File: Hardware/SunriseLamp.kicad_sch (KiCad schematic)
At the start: 0 parts

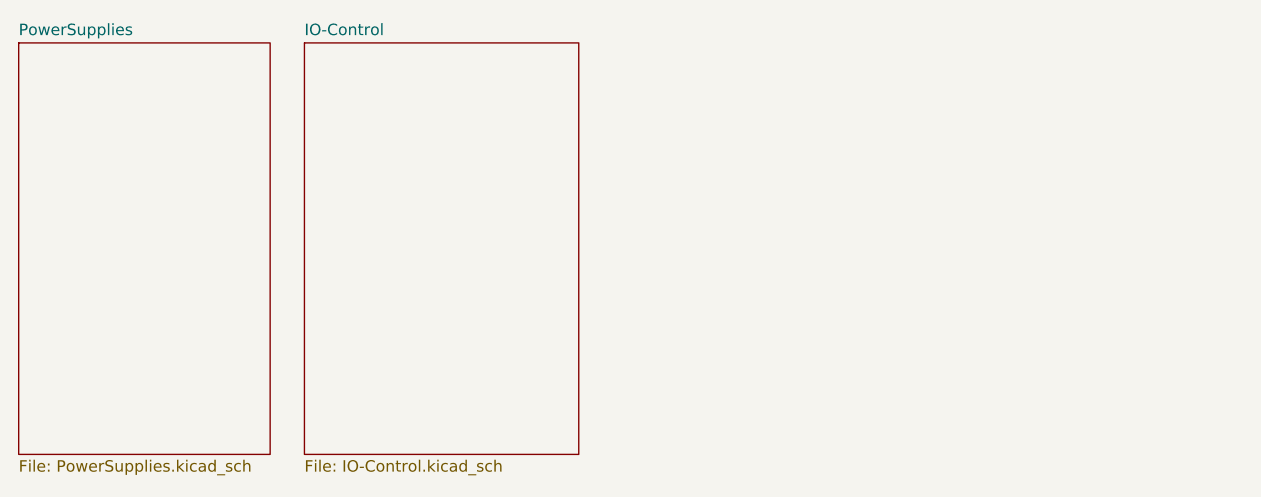
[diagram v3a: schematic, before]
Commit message: USB footprint added, mount holes added.
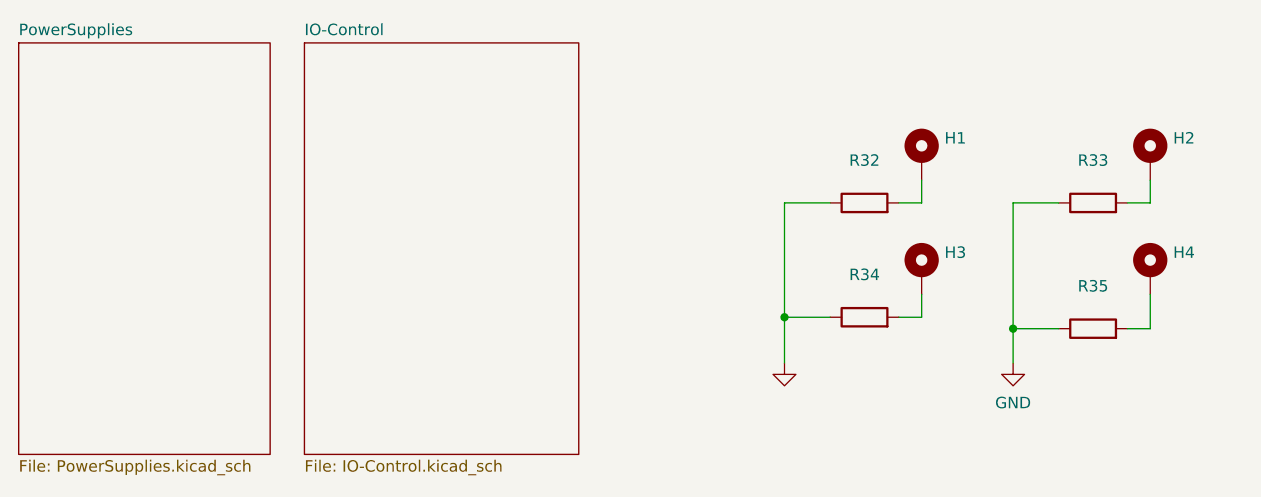
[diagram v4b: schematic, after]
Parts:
- added H1, H2, H3, H4: (no value), symbol Mechanical:MountingHole_Pad
- added R32, R33, R34, R35: (no value), symbol Device:R
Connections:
- new net: H3.1, R34.2
- new net: H1.1, R32.2
- new net: H4.1, R35.2
- new net: H2.1, R33.2
- new net GND: R32.1, R33.1, R34.1, R35.1

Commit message: Whoops, acidentally wiped all part assignments somehow. corrected.
Only pending footprint creation is for two switches.
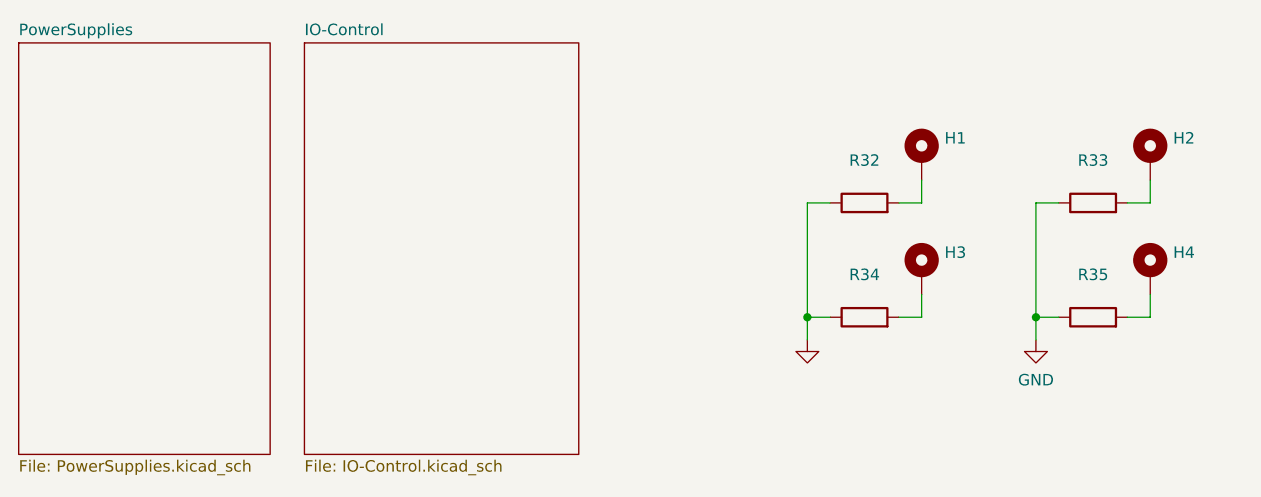
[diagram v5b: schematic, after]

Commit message: Layout changes
Changed XT60 outputs to Mini-Fit Jr., laid out 80mm fan edge cuts, started positioning conns
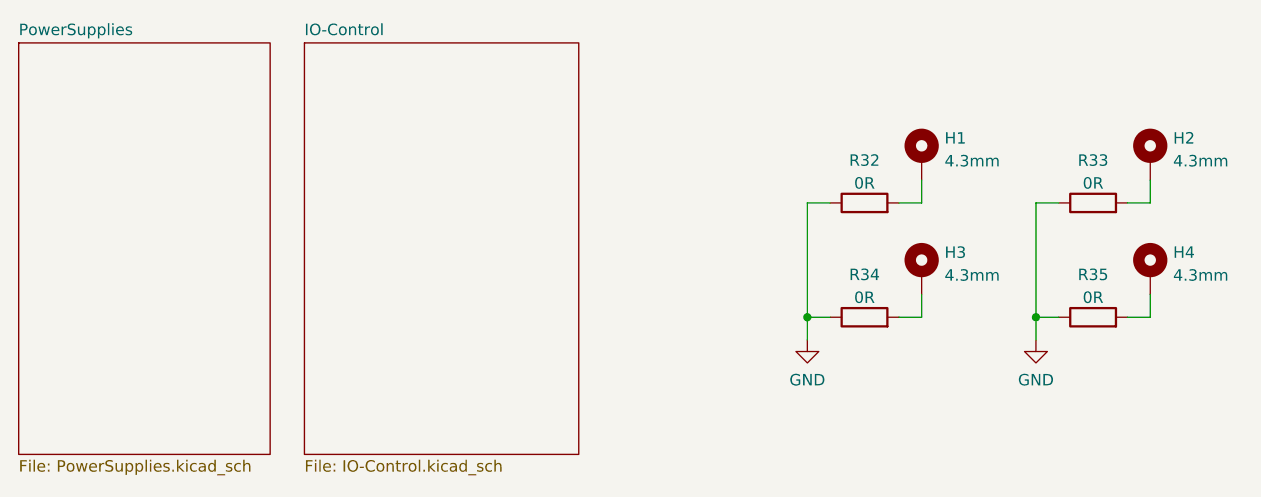
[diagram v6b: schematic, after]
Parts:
- H1, H2, H3, H4: value (none) -> 4.3mm; footprint (none) -> MountingHole:MountingHole_4.3mm_M4_DIN965_Pad_TopBottom
- R32, R33, R34, R35: value (none) -> 0R; footprint (none) -> Resistor_SMD:R_0805_2012Metric_Pad1.20x1.40mm_HandSolder
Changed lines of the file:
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@@
     (in_bom yes) (on_board yes) (fields_autoplaced)
     (property "Reference" "R35" (id 0) (at 146.05 52.4342 90))
-    (property "Value" "" (id 1) (at 146.05 54.9711 90))
-    (property "Footprint" "" (id 2) (at 146.05 58.928 90)
+    (property "Value" "0R" (id 1) (at 146.05 54.9711 90))
+    (property "Footprint" "Resistor_SMD:R_0805_2012Metric_Pad1.20x1.40mm_HandSolder" (id 2) (at 146.05 58.928 90)
       (effects (font (size 1.27 1.27)) hide)
     )
@@
     (in_bom yes) (on_board yes) (fields_autoplaced)
     (property "Reference" "R34" (id 0) (at 120.65 52.4342 90))
-    (property "Value" "" (id 1) (at 120.65 54.9711 90))
-    (property "Footprint" "" (id 2) (at 120.65 58.928 90)
+    (property "Value" "0R" (id 1) (at 120.65 54.9711 90))
+    (property "Footprint" "Resistor_SMD:R_0805_2012Metric_Pad1.20x1.40mm_HandSolder" (id 2) (at 120.65 58.928 90)
       (effects (font (size 1.27 1.27)) hide)
     )
@@
     (in_bom yes) (on_board yes) (fields_autoplaced)
     (property "Reference" "R33" (id 0) (at 146.05 39.7342 90))
-    (property "Value" "" (id 1) (at 146.05 42.2711 90))
-    (property "Footprint" "" (id 2) (at 146.05 46.228 90)
+    (property "Value" "0R" (id 1) (at 146.05 42.2711 90))
+    (property "Footprint" "Resistor_SMD:R_0805_2012Metric_Pad1.20x1.40mm_HandSolder" (id 2) (at 146.05 46.228 90)
       (effects (font (size 1.27 1.27)) hide)
     )
@@
       (effects (font (size 1.27 1.27)) (justify left))
     )
-    (property "Value" "" (id 1) (at 129.54 39.8022 0)
-      (effects (font (size 1.27 1.27)) (justify left))
-    )
-    (property "Footprint" "" (id 2) (at 127 39.37 0)
+    (property "Value" "4.3mm" (id 1) (at 129.54 39.8022 0)
+      (effects (font (size 1.27 1.27)) (justify left))
+    )
+    (property "Footprint" "MountingHole:MountingHole_4.3mm_M4_DIN965_Pad_TopBottom" (id 2) (at 127 39.37 0)
       (effects (font (size 1.27 1.27)) hide)
     )
@@
       (effects (font (size 1.27 1.27)) (justify left))
     )
-    (property "Value" "" (id 1) (at 154.94 39.8022 0)
-      (effects (font (size 1.27 1.27)) (justify left))
-    )
-    (property "Footprint" "" (id 2) (at 152.4 39.37 0)
+    (property "Value" "4.3mm" (id 1) (at 154.94 39.8022 0)
+      (effects (font (size 1.27 1.27)) (justify left))
+    )
+    (property "Footprint" "MountingHole:MountingHole_4.3mm_M4_DIN965_Pad_TopBottom" (id 2) (at 152.4 39.37 0)
       (effects (font (size 1.27 1.27)) hide)
     )
@@
       (effects (font (size 1.27 1.27)) hide)
     )
-    (property "Value" "" (id 1) (at 114.3 64.1334 0))
+    (property "Value" "GND" (id 1) (at 114.3 64.1334 0))
     (property "Footprint" "" (id 2) (at 114.3 59.69 0)
       (effects (font (size 1.27 1.27)) hide)
@@
       (effects (font (size 1.27 1.27)) (justify left))
     )
-    (property "Value" "" (id 1) (at 129.54 52.5022 0)
-      (effects (font (size 1.27 1.27)) (justify left))
-    )
-    (property "Footprint" "" (id 2) (at 127 52.07 0)
+    (property "Value" "4.3mm" (id 1) (at 129.54 52.5022 0)
+      (effects (font (size 1.27 1.27)) (justify left))
+    )
+    (property "Footprint" "MountingHole:MountingHole_4.3mm_M4_DIN965_Pad_TopBottom" (id 2) (at 127 52.07 0)
       (effects (font (size 1.27 1.27)) hide)
     )
@@
       (effects (font (size 1.27 1.27)) (justify left))
     )
-    (property "Value" "" (id 1) (at 154.94 52.5022 0)
-      (effects (font (size 1.27 1.27)) (justify left))
-    )
-    (property "Footprint" "" (id 2) (at 152.4 52.07 0)
+    (property "Value" "4.3mm" (id 1) (at 154.94 52.5022 0)
+      (effects (font (size 1.27 1.27)) (justify left))
+    )
+    (property "Footprint" "MountingHole:MountingHole_4.3mm_M4_DIN965_Pad_TopBottom" (id 2) (at 152.4 52.07 0)
       (effects (font (size 1.27 1.27)) hide)
     )
@@
     (in_bom yes) (on_board yes) (fields_autoplaced)
     (property "Reference" "R32" (id 0) (at 120.65 39.7342 90))
-    (property "Value" "" (id 1) (at 120.65 42.2711 90))
-    (property "Footprint" "" (id 2) (at 120.65 46.228 90)
+    (property "Value" "0R" (id 1) (at 120.65 42.2711 90))
+    (property "Footprint" "Resistor_SMD:R_0805_2012Metric_Pad1.20x1.40mm_HandSolder" (id 2) (at 120.65 46.228 90)
       (effects (font (size 1.27 1.27)) hide)
     )
@@
       (reference "J2") (unit 1) (value "S3B-XH-A") (footprint "Connector_JST:JST_XH_S3B-XH-A-1_1x03_P2.50mm_Horizontal")
     )
+    (path "/7af2029e-2b92-4284-9c35-cc656514173c/ecb680b0-e8a8-4eac-a1b3-9b317b6f69d6"
+      (reference "J3") (unit 1) (value "Molex 26013114") (footprint "Connector_Molex:Molex_Mini-Fit_Jr_5569-02A2_2x01_P4.20mm_Horizontal")
+    )
+    (path "/7af2029e-2b92-4284-9c35-cc656514173c/14828e08-67cc-4111-ab74-390df006b759"
+      (reference "J4") (unit 1) (value "Molex 26013114") (footprint "Connector_Molex:Molex_Mini-Fit_Jr_5569-02A2_2x01_P4.20mm_Horizontal")
+    )
+    (path "/7af2029e-2b92-4284-9c35-cc656514173c/269b3901-4985-48dd-bb36-3dfe77ba1464"
+      (reference "J5") (unit 1) (value "Molex 26013114") (footprint "Connector_Molex:Molex_Mini-Fit_Jr_5569-02A2_2x01_P4.20mm_Horizontal")
+    )
+    (path "/7af2029e-2b92-4284-9c35-cc656514173c/94cd80bb-b901-4fe9-bb1a-09f8a7fdaa98"
+      (reference "J6") (unit 1) (value "Molex 26013114") (footprint "Connector_Molex:Molex_Mini-Fit_Jr_5569-02A2_2x01_P4.20mm_Horizontal")
+    )
     (path "/7af2029e-2b92-4284-9c35-cc656514173c/9f095dd4-7522-4f5e-8dbd-36a8a511cb15"
       (reference "L1") (unit 1) (value "33u 2A") (footprint "Inductor_SMD:L_SigTra_SC3316F")
@@
       (reference "P1") (unit 1) (value "XT60PW-M") (footprint "PersonalConnectors:AMASS_XT60PW-M")
     )
-    (path "/7af2029e-2b92-4284-9c35-cc656514173c/1c5ce8c9-e1ce-4e63-a99a-5463370a0b98"
-      (reference "P2") (unit 1) (value "XT60PW-F") (footprint "PersonalConnectors:AMASS_XT60PW-F")
-    )
-    (path "/7af2029e-2b92-4284-9c35-cc656514173c/c947d341-044e-4a95-90db-024433f36611"
-      (reference "P3") (unit 1) (value "XT60PW-F") (footprint "PersonalConnectors:AMASS_XT60PW-F")
-    )
-    (path "/7af2029e-2b92-4284-9c35-cc656514173c/ab1fe289-346d-4ee7-84cc-1eb030bab9bd"
-      (reference "P4") (unit 1) (value "XT60PW-F") (footprint "PersonalConnectors:AMASS_XT60PW-F")
-    )
-    (path "/7af2029e-2b92-4284-9c35-cc656514173c/8d936772-f6fa-4d42-bb01-ee988a455edf"
-      (reference "P5") (unit 1) (value "XT60PW-F") (footprint "PersonalConnectors:AMASS_XT60PW-F")
-    )
     (path "/e03b0f56-1755-48ae-848f-a899b33ab61d/8b8d16cf-c006-49ad-9970-e3d988d42355"
